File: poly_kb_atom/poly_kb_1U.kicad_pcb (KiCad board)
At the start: 2 copper layers, 19 x 19 mm, 38 parts, among them J1 Conn_01x16, J2 North, J3 WestFront, J4 EastFront, J5 WestBack, J6 EastBack, J7 South, J8 North2, J9 South2, SW1 SW_Push

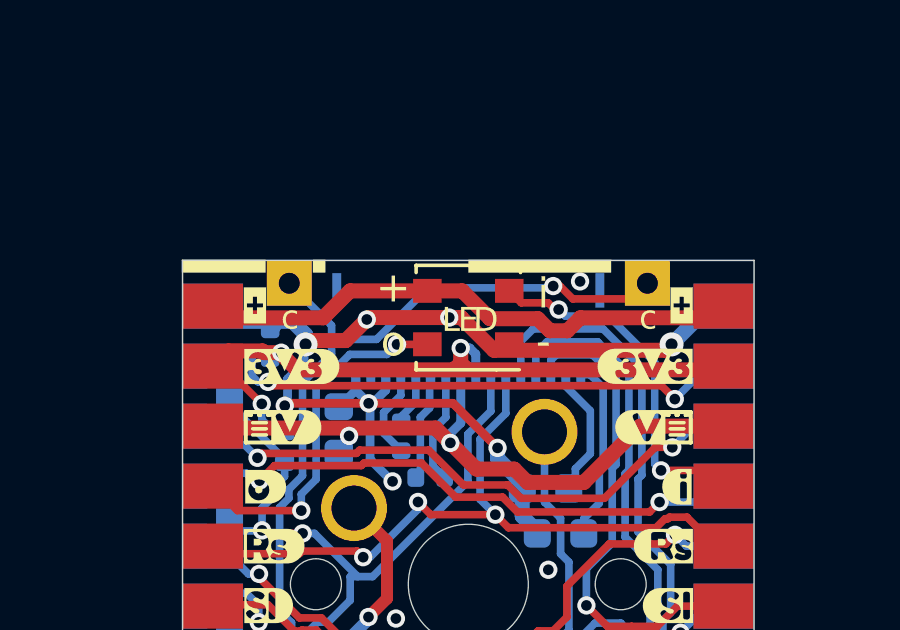
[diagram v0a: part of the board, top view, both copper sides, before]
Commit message: Added optional C7 and fix LED silkscreens
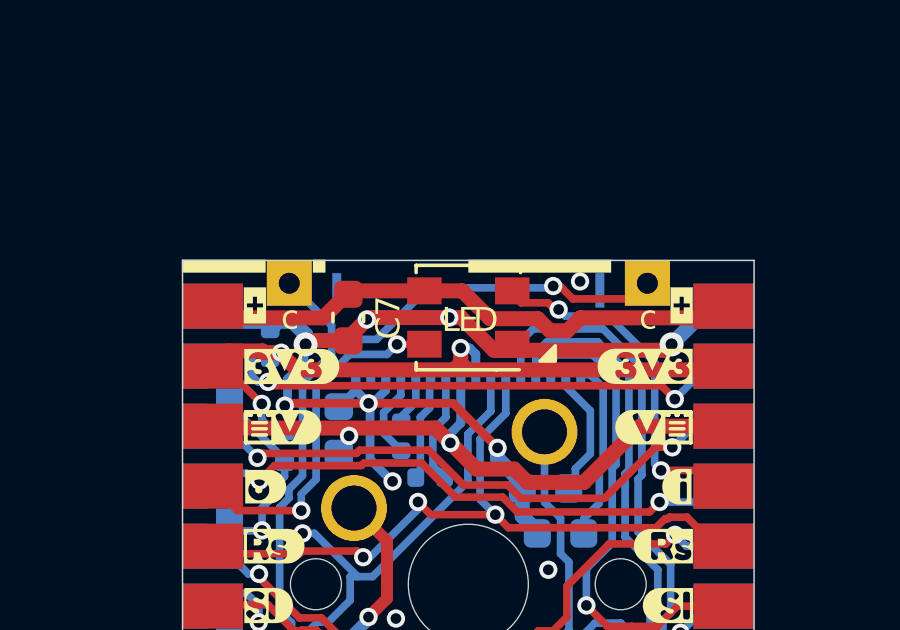
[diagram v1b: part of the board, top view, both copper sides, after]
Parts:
- added C7: 100nF, Capacitor_SMD:C_0603_1608Metric, F.Cu at (97.7, 56.1)
- LED1: value LED -> WS2812B-Mini
